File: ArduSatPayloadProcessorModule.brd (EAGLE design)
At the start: 95.5 x 90.3 mm, 335 parts, among them IC1 ATMEGA328P QFN32, IC10 ATMEGA328P QFN32, IC11 ATMEGA328P QFN32, IC12 ATMEGA328P QFN32, IC13 ATMEGA328P QFN32, IC14 ATMEGA328P QFN32, IC15 ATMEGA328P QFN32, IC16 ATMEGA328P QFN32, IC17 TXB0104, IC18 TMP102, IC19 TMP102, IC2 ATMEGA328P QFN32, IC20 ATMEGA2561-16MU, IC21 MAX4372F, IC22 MAX4372F, IC23 MUX-74HC4067-QFNSMT, IC24 MUX-74HC4067-QFNSMT, IC3 ATMEGA328P QFN32, IC4 ATMEGA328P QFN32, IC5 ATMEGA328P QFN32, IC6 ATMEGA328P QFN32, IC7 ATMEGA328P QFN32, IC8 ATMEGA328P QFN32, IC9 ATMEGA328P QFN32, P1 microSD, Q1 RJU003N03 N-MOSFET, Q10 RJU003N03 N-MOSFET, Q11 RJU003N03 N-MOSFET, Q12 RJU003N03 N-MOSFET, Q13 RJU003N03 N-MOSFET, Q14 RJU003N03 N-MOSFET, Q15 RJU003N03 N-MOSFET, Q16 RJU003N03 N-MOSFET, Q17 RJU003N03 N-MOSFET, Q18 RJU003N03 N-MOSFET, Q19 RJU003N03 N-MOSFET, Q2 RJU003N03 N-MOSFET, Q20 RJU003N03 N-MOSFET, Q21 RJU003N03 N-MOSFET, Q22 RJU003N03 N-MOSFET, Q23 RJU003N03 N-MOSFET, Q24 RJU003N03 N-MOSFET, Q25 RJU003N03 N-MOSFET, Q26 RJU003N03 N-MOSFET, Q27 RJU003N03 N-MOSFET, Q28 RJU003N03 N-MOSFET, Q29 RJU003N03 N-MOSFET, Q3 RJU003N03 N-MOSFET, Q30 RJU003N03 N-MOSFET, Q31 RJU003N03 N-MOSFET, Q32 RJU003N03 N-MOSFET, Q33 RJU003N03 N-MOSFET, Q34 RJU003N03 N-MOSFET, Q35 RJU003N03 N-MOSFET, Q36 RJU003N03 N-MOSFET, Q37 RJU003N03 N-MOSFET, Q38 RJU003N03 N-MOSFET, Q39 RJU003N03 N-MOSFET, Q4 RJU003N03 N-MOSFET, Q40 RJU003N03 N-MOSFET, Q41 RJU003N03 N-MOSFET, Q42 RJU003N03 N-MOSFET, Q43 RJU003N03 N-MOSFET, Q44 RJU003N03 N-MOSFET, Q45 RJU003N03 N-MOSFET, Q46 RJU003N03 N-MOSFET, Q5 RJU003N03 N-MOSFET, Q6 RJU003N03 N-MOSFET, Q7 RJU003N03 N-MOSFET, Q8 RJU003N03 N-MOSFET, Q9 RJU003N03 N-MOSFET, SW1 ADG801 SOT23-6, SW10 ADG801 SOT23-6, SW11 ADG801 SOT23-6, SW12 ADG801 SOT23-6, SW13 ADG801 SOT23-6, SW14 ADG801 SOT23-6, SW15 ADG801 SOT23-6, SW16 ADG801 SOT23-6, SW17 RESET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

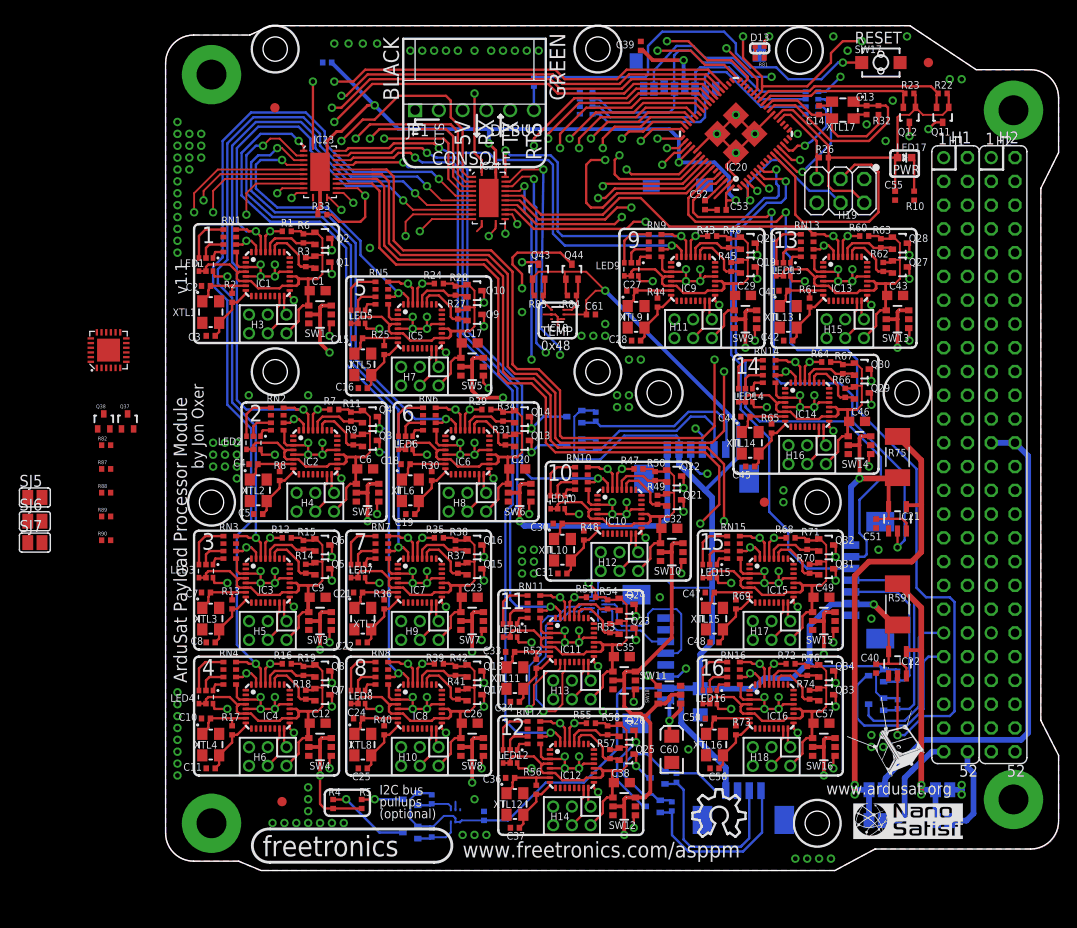
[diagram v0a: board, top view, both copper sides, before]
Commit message: Start of placement and fan-out of node reset latch
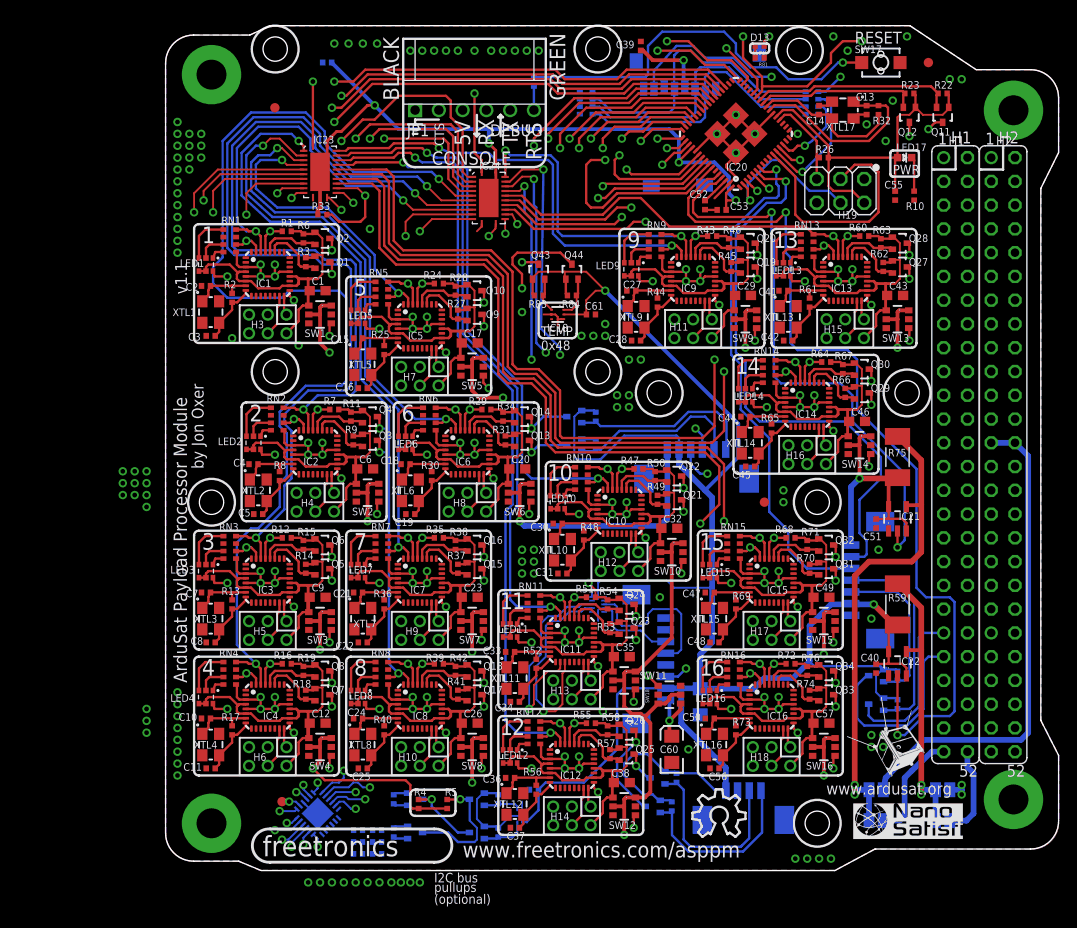
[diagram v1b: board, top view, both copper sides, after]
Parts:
- SJ5, SJ6, SJ7: device freetronics-master-v1:SJ -> freetronics-jon:0402SJO
- moved U$26 54.3 mm to (16.3, 6.10), flipped to the bottom, turned to 45 degrees
- moved Q37 53.6 mm to (26.7, 4.06), flipped to the bottom, turned to 90 degrees
- moved Q38 52.3 mm to (26.7, 7.62), flipped to the bottom, turned to 90 degrees
- moved R82 51.6 mm to (24.4, 4.06), flipped to the bottom, turned to 270 degrees
- moved SJ5 49.6 mm to (20.6, 4.32), flipped to the bottom
- moved SJ6 48.7 mm to (20.6, 3.05), flipped to the bottom
- moved R88 48.3 mm to (22.6, 1.78), flipped to the bottom
- moved SJ7 48.0 mm to (20.6, 1.78), flipped to the bottom
- moved R87 46.8 mm to (24.4, 7.62), flipped to the bottom, turned to 270 degrees
- moved R89 45.3 mm to (22.6, 3.05), flipped to the bottom
- moved R90 42.4 mm to (22.6, 4.32), flipped to the bottom
- moved R5 9.14 mm to (30.1, 7.11)
- moved R4 9.14 mm to (27.1, 7.11)
- moved IC19 7.11 mm to (38.1, 5.84)
- moved Q45 7.11 mm to (33.3, 7.62)
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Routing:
- net N4_D0_RX: track 96.5 -> 116.3 mm
- net N3_D0_RX: track 80.7 -> 97.7 mm
- net SCL: track 393.5 -> 409.0 mm
- net 5V: track 588.8 -> 602.3 mm
- net N2_D0_RX: track 70.7 -> 80.4 mm
- net N13_RESET: track 13.6 -> 19.7 mm, vias 1 -> 2
- net 3.3V: track 283.8 -> 278.0 mm
- net SDA: track 424.0 -> 428.7 mm
- net N12_RESET: track 13.6 -> 18.1 mm, vias 1 -> 2
- net N15_RESET: track 13.6 -> 18.0 mm, vias 1 -> 2
- net N14_RESET: track 13.6 -> 17.3 mm, vias 1 -> 2
- net N5_RESET: track 13.6 -> 17.2 mm, vias 1 -> 2
- net N4_RESET: track 13.6 -> 17.0 mm, vias 1 -> 2
- net N3_RESET: track 13.6 -> 16.8 mm, vias 1 -> 2
- net N16_RESET: track 13.6 -> 16.8 mm, vias 1 -> 2
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
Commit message: Finished routing latch for resetting nodes
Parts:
- moved R90 8.32 mm to (29.7, 8.64)
- moved R89 6.12 mm to (16.5, 2.54), flipped to the top
- moved R88 5.86 mm to (16.8, 1.27), turned to 180 degrees
- moved SJ5 1.70 mm to (22.1, 5.08), turned to 180 degrees
- moved SJ7 1.61 mm to (22.1, 1.27), turned to 180 degrees
- moved SJ6 1.52 mm to (22.1, 3.05), turned to 180 degrees
- moved Q38 0.25 mm to (26.7, 7.37)
- moved R87 0.25 mm to (24.4, 7.37)
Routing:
- net N13_RESET: track 19.7 -> 150.9 mm, vias 2 -> 4
- net N9_RESET: track 15.5 -> 129.3 mm, vias 2 -> 4
- net N5_RESET: track 17.2 -> 106.9 mm, vias 2 -> 1
- net N14_RESET: track 17.3 -> 104.9 mm, vias 2 -> 4
- net N10_RESET: track 15.6 -> 87.0 mm, vias 2 -> 3
- net N1_RESET: track 15.3 -> 83.6 mm, vias 2 -> 1
- net N15_RESET: track 18.0 -> 80.6 mm, vias 2 -> 4
- net N6_RESET: track 15.4 -> 69.2 mm, vias 2 -> 1
- net N16_RESET: track 16.8 -> 66.8 mm
- net N11_RESET: track 15.1 -> 62.2 mm, vias 2 -> 1
- net N2_RESET: track 15.8 -> 62.4 mm
- net N3_RESET: track 16.8 -> 53.2 mm, vias 2 -> 1
- net N7_RESET: track 16.0 -> 49.1 mm
- net N12_RESET: track 18.1 -> 44.5 mm, vias 2 -> 1
- net 5V: track 602.3 -> 622.4 mm, vias 18 -> 19
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
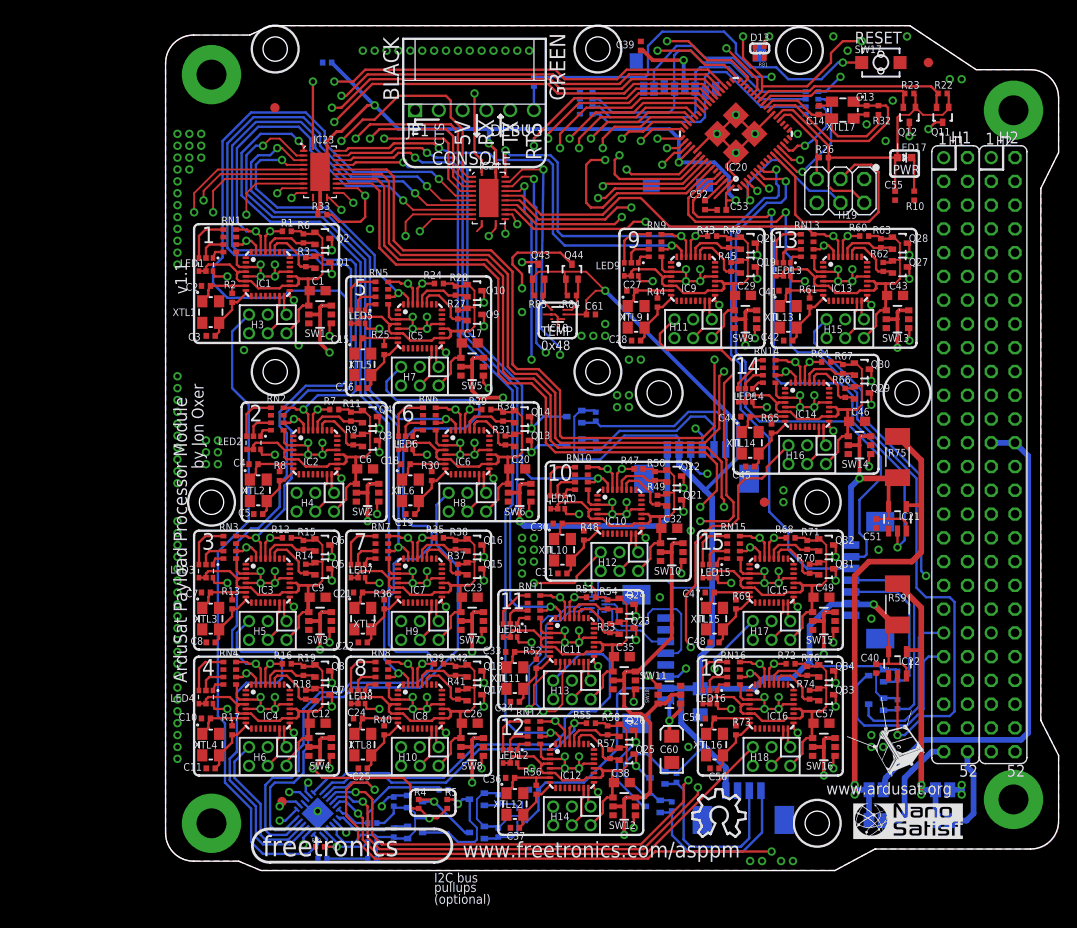
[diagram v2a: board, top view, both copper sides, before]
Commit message: Clearance and label improvements
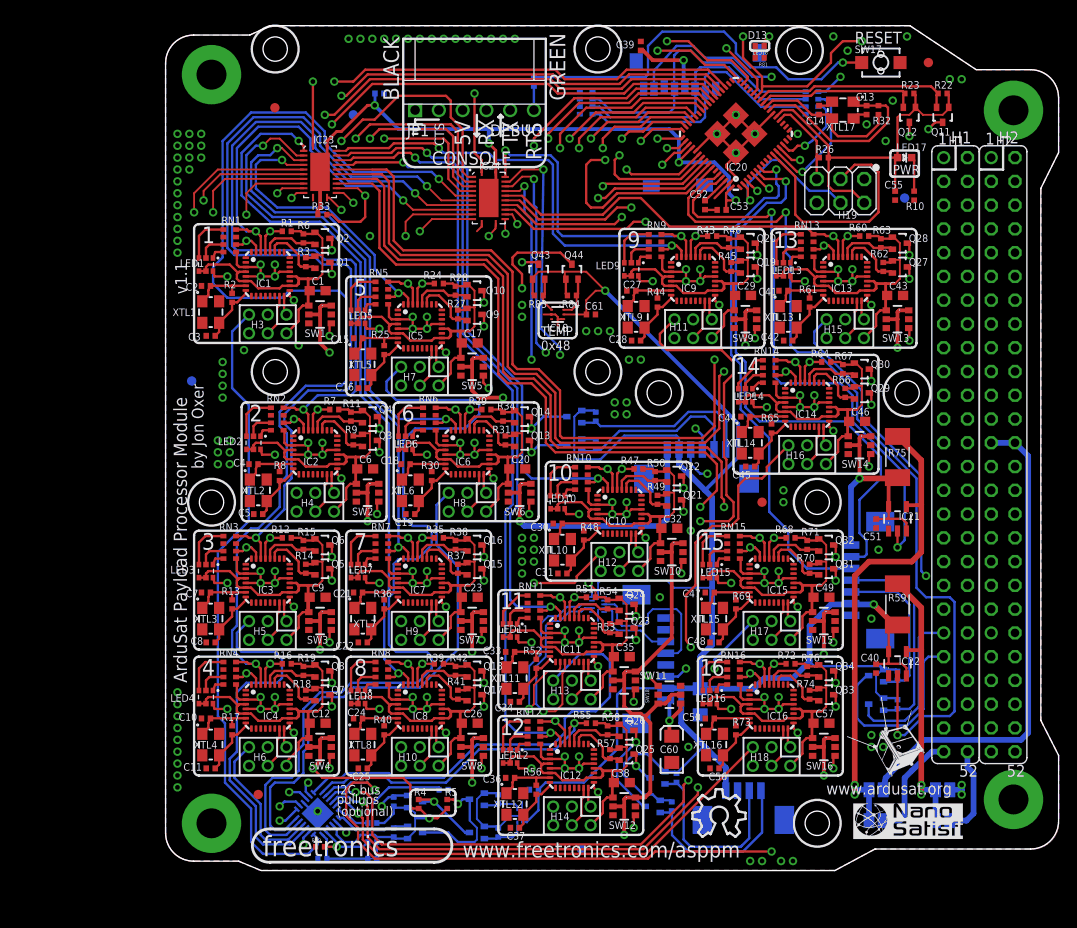
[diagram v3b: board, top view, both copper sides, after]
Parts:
- added FID5, FID6, FID7, FID8: FIDUCIAL1X2.5, freetronics:FIDUCIAL-1X2.5
- SJ7: value (none) -> SJC0402; device freetronics-jon:0402SJO -> freetronics-jon:0402SJC
- moved C54 6.49 mm to (22.9, 83.1), turned to 180 degrees
- moved FID4 2.65 mm to (9.91, 8.13)
- moved FID3 0.25 mm to (63.8, 39.4)
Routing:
- net 5V: track 622.4 -> 617.2 mm
- net GND: vias 184 -> 165
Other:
- board text added: "0x24"
- board text added: "A0"
- board text added: "A1"
- board text added: "A2"
- board text added: "ADDR"
- board text added: "DEFAULT"
- board text added: "LATCH"
- board text added: "NODE"

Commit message: Re-routed around MCU GND pads and improved footprints
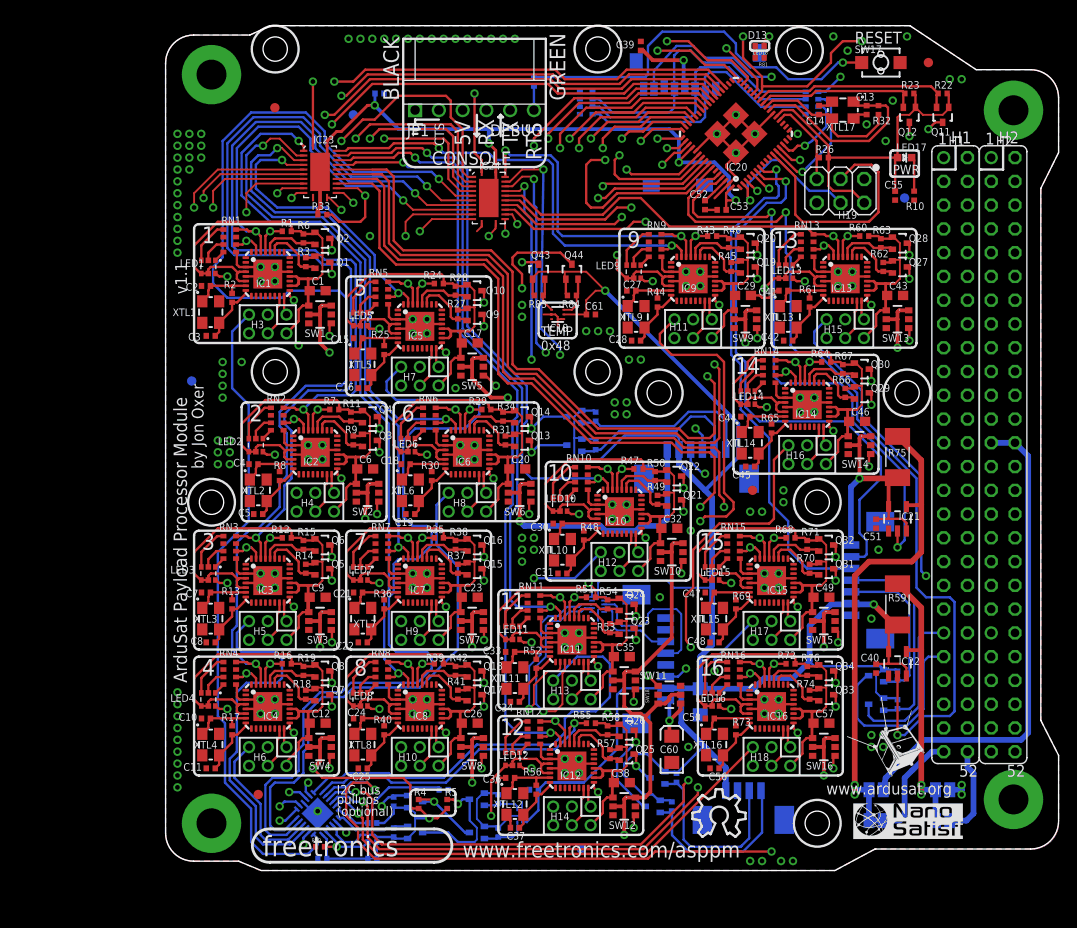
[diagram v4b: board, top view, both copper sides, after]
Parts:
- IC1, IC10, IC11, IC12, IC13, IC14, IC15, IC16, IC2, IC3, IC4, IC5, IC6, IC7, IC8, IC9: device freetronics-master-v1.1:MLF32 -> freetronics-jon:MLF32
- moved FID3 1.63 mm to (62.7, 40.6)
- moved LED11 0.36 mm to (37.1, 25.4)
- moved LED16 0.36 mm to (58.4, 18.3)
- moved LED12 0.36 mm to (37.1, 11.9)
- moved LED10 0.36 mm to (42.2, 39.1)
- moved LED15 0.36 mm to (58.4, 31.8)
- moved LED5 0.36 mm to (20.8, 58.9)
- moved LED9 0.36 mm to (50.0, 64.0)
- moved LED4 0.36 mm to (4.57, 18.3)
- moved LED6 0.36 mm to (25.9, 45.5)
- moved LED8 0.36 mm to (20.8, 18.3)
- moved LED3 0.36 mm to (4.57, 31.8)
- moved LED2 0.36 mm to (9.65, 45.5)
- moved LED14 0.36 mm to (62.2, 50.5)
- moved LED7 0.36 mm to (20.8, 31.8)
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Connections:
- net GND: now also IC1.TGND, IC10.TGND, IC11.TGND, IC12.TGND, IC13.TGND, IC14.TGND, IC15.TGND, IC16.TGND, IC2.TGND, IC3.TGND, IC4.TGND, IC5.TGND, IC6.TGND, IC7.TGND, IC8.TGND, IC9.TGND
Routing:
- net GND: track 224.9 -> 273.5 mm, vias 165 -> 166
- net N9_5V: track 35.4 -> 50.6 mm, vias 0 -> 1
- net N12_5V: track 35.4 -> 48.1 mm, vias 0 -> 1
- net N16_5V: track 35.4 -> 46.2 mm
- net N13_5V: track 35.4 -> 46.0 mm, vias 0 -> 1
- net N10_5V: track 35.4 -> 45.6 mm
- net N15_5V: track 35.4 -> 45.6 mm
- net N8_5V: track 35.4 -> 45.6 mm
- net N2_5V: track 35.4 -> 45.6 mm
- net N14_5V: track 35.4 -> 45.6 mm
- net N5_5V: track 35.4 -> 45.6 mm
- net N3_5V: track 35.4 -> 45.6 mm
- net N7_5V: track 35.4 -> 45.6 mm
- net N1_5V: track 35.4 -> 45.6 mm
- net N4_5V: track 35.4 -> 45.6 mm
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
